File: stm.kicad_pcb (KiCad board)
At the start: 2 copper layers, 39.9 x 18 mm, 28 parts, among them J1 USB_B_Micro, J2 Conn_01x04_Pin, J3 Conn_01x04_Pin, J4 Conn_01x04_Pin, SW1 SW_SPDT, U1 AMS1117-3.3, U2 STM32F103C8Tx, Y1 16MHz

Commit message: changed layout design
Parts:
- added H1: MountingHole, MountingHole:MountingHole_2.1mm, F.Cu at (56.2, 94.8)
- added H2: MountingHole, MountingHole:MountingHole_2.1mm, F.Cu at (89.1, 94.8)
- added H3: MountingHole, MountingHole:MountingHole_2.1mm, F.Cu at (56.2, 115.5)
- added H4: MountingHole, MountingHole:MountingHole_2.1mm, F.Cu at (89.1, 115.5)
- SW1: footprint Button_Switch_SMD:Nidec_Copal_CAS-120A -> Button_Switch_SMD:SW_SPST_B3U-1100P-B
- moved R2 94.2 mm to (65.1, 107.5), turned to 90 degrees
- moved R3 90.4 mm to (68.4, 102.9), turned to 90 degrees
- moved R5 85.6 mm to (73.3, 98.9), turned to 180 degrees
- moved R4 83.1 mm to (75.7, 98.9)
- moved R1 79.3 mm to (80.7, 109.5)
- moved C5 74.9 mm to (62.6, 100.7), turned to 180 degrees
- moved D1 31.3 mm to (66.3, 103.6), turned to 90 degrees
- moved J4 26.9 mm to (78.2, 94.2), turned to -90 degrees
- moved C6 26.1 mm to (64.8, 111.5)
- moved SW1 21.1 mm to (85.0, 111.5), turned to 90 degrees
- moved C4 13.2 mm to (66.4, 100.7), turned to 180 degrees
- moved U1 11.8 mm to (64.0, 96.0), turned to 180 degrees
- moved J2 10.4 mm to (62.4, 116.1)
- moved J3 9.72 mm to (73.8, 116.1)
- moved C11 6.94 mm to (81.7, 103.4)
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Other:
- board size 39.9 x 18 mm -> 38.9 x 26.7 mm

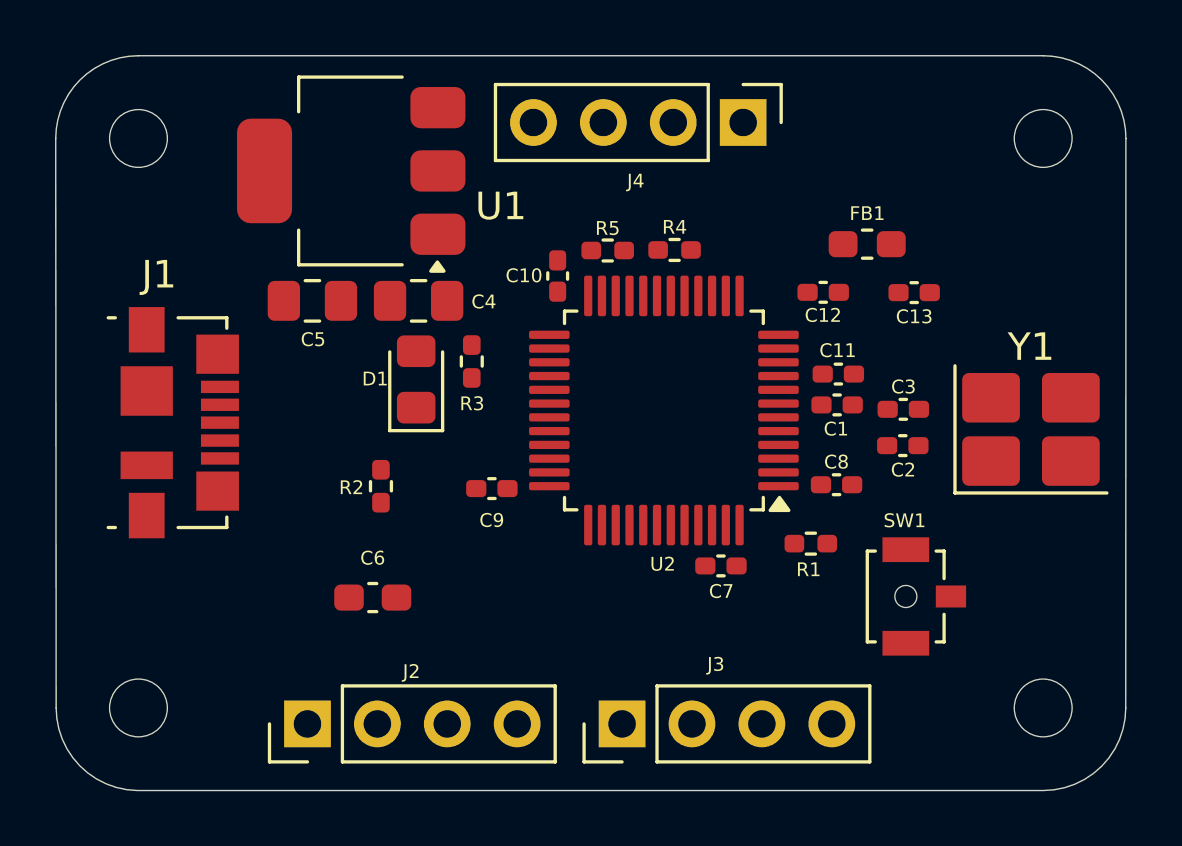
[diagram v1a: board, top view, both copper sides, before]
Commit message: added routing, need to change size of pwr routes and connect all GND to gnd plane
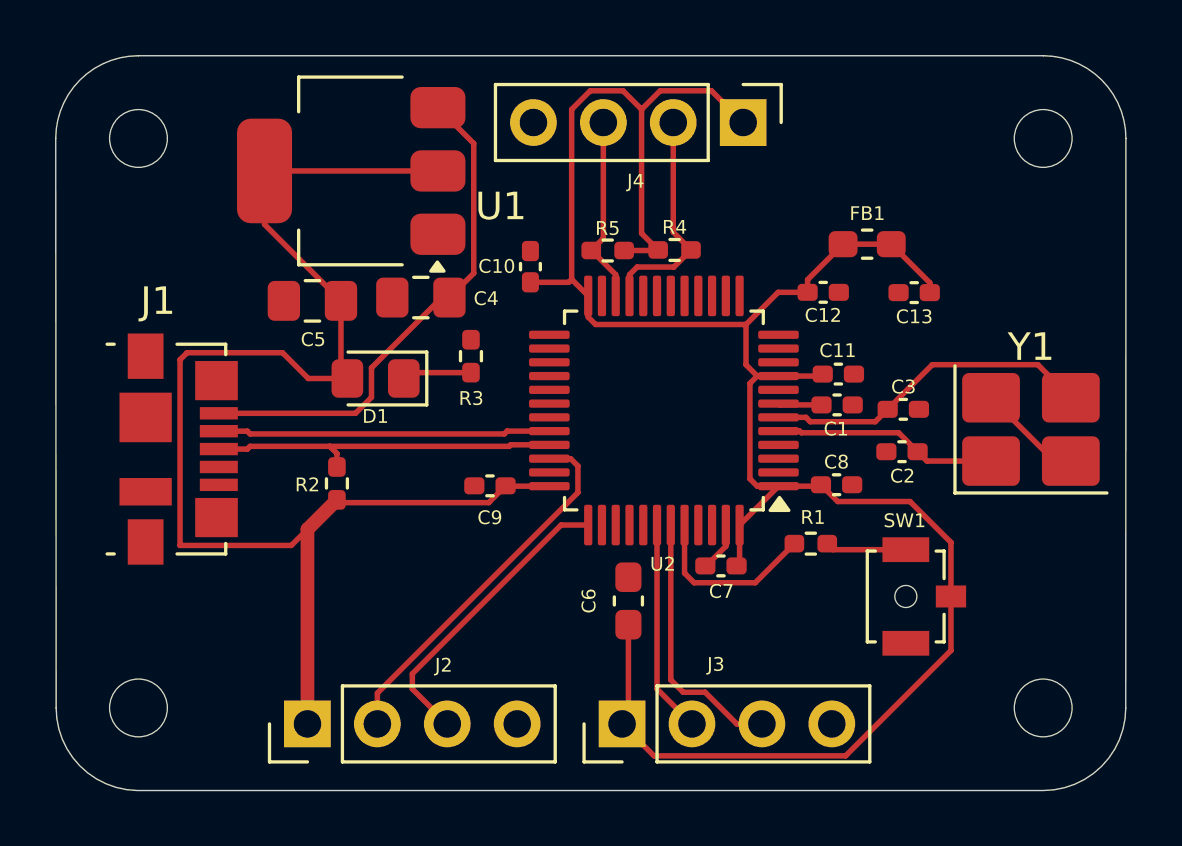
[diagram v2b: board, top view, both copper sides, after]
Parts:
- moved C6 9.29 mm to (74.0, 111.6), turned to 90 degrees
- moved R2 1.60 mm to (63.5, 107.4)
- moved D1 1.48 mm to (64.9, 103.5), turned to 180 degrees
- moved C10 1.05 mm to (70.5, 99.5)
- moved J1 0.96 mm to (57.7, 106.1)
- moved C2 0.22 mm to (84.0, 106.2)
- moved R3 0.19 mm to (68.3, 102.7)
- moved C4 0.15 mm to (66.5, 100.6)
- moved C9 0.12 mm to (69.0, 107.5)
- turned R1 to 180 degrees
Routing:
- net +3.3V: track 0.00 -> 132.4 mm
- net VBUS: track 0.00 -> 18.6 mm
- net /SWDIO: track 0.00 -> 13.5 mm
- net /USB_D+: track 0.00 -> 12.9 mm
- net /USB_D-: track 0.00 -> 12.1 mm
- net /HSE_OUT: track 0.00 -> 12.0 mm
- net /SWCLK: track 0.00 -> 11.0 mm
- net /UART_RX: track 0.00 -> 9.60 mm
- net /I2C2_SCL: track 0.00 -> 8.28 mm
- net /HSE_IN: track 0.00 -> 8.17 mm
- net /UART_TX: track 0.00 -> 7.75 mm
- net /I2C2_SDA: track 0.00 -> 6.86 mm
- net /Boot0: track 0.00 -> 6.47 mm
- net GND: track 0.00 -> 5.66 mm
- net /SW_boot0: track 0.00 -> 2.95 mm
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
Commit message: done with proj
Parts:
- moved C10 0.86 mm to (71.3, 99.7)
- moved C4 0.12 mm to (66.4, 100.6)
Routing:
- net GND: track 5.66 -> 61.0 mm, vias 0 -> 14
- net +3.3V: track 132.4 -> 143.0 mm, vias 0 -> 4
- net VBUS: track 18.6 -> 22.4 mm
- added copper zone on B.Cu, net GND
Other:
- board text added: "By: Nikunj Shah :>"
- board text added: "STM32 basic microcontroller"
